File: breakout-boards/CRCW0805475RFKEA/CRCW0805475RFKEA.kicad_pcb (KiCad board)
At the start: 2 copper layers, 14 parts, among them J1 Conn_01x12, J2 Conn_01x12

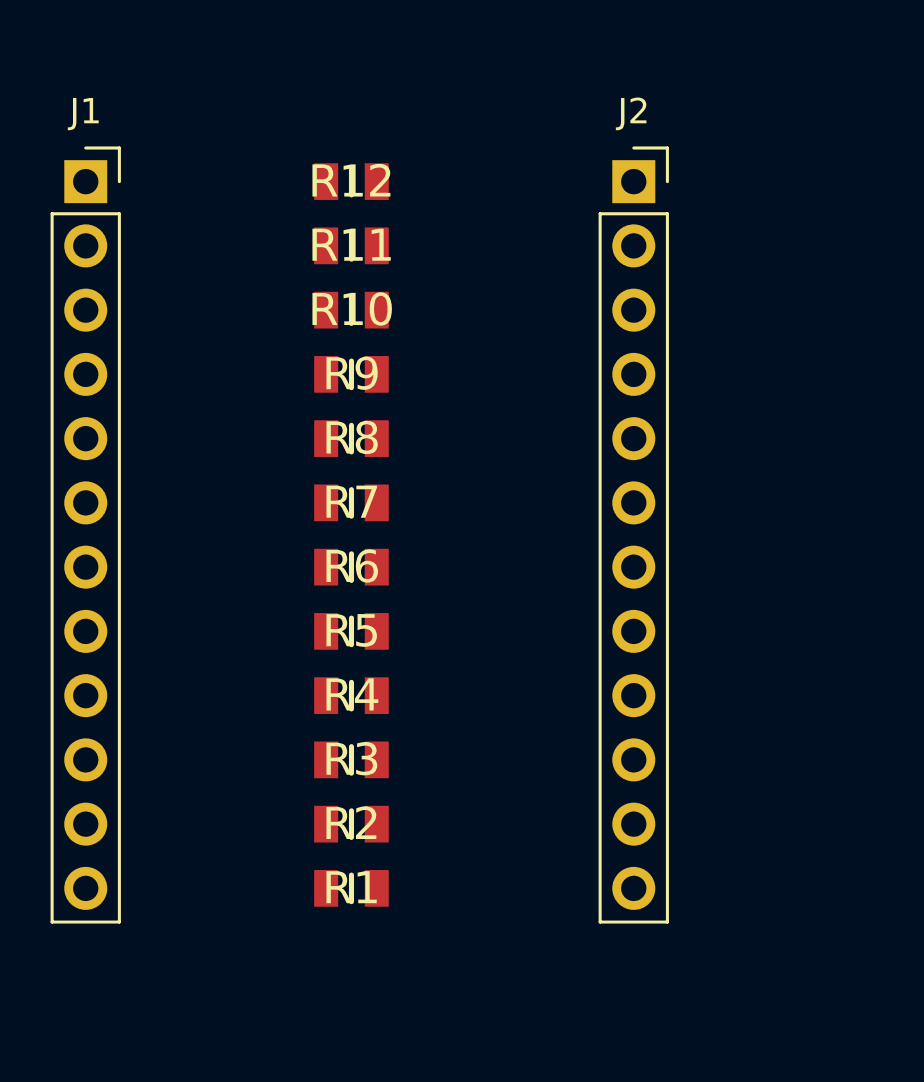
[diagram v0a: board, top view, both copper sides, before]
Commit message: feat: create footprints for resistor breakout boards
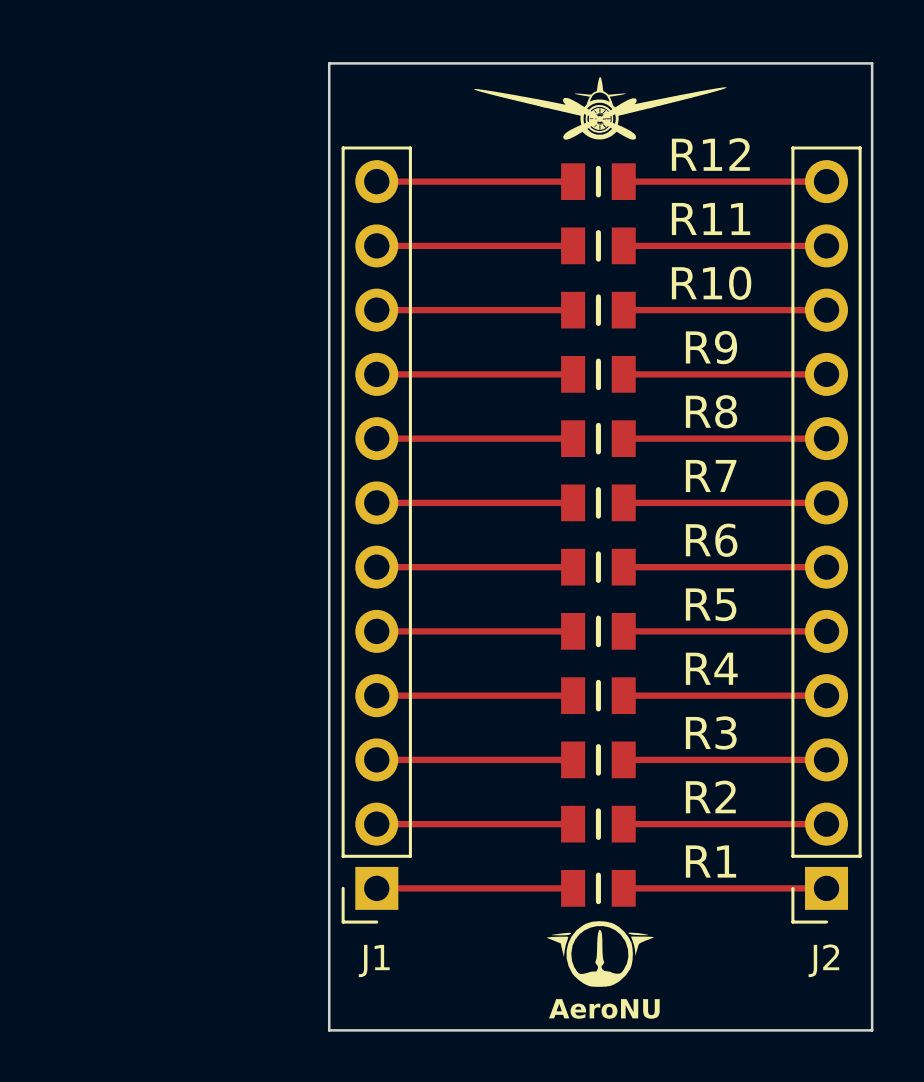
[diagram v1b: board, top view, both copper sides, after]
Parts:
- added AeroNU: LOGO, FixedWing:AeroNU - Logo (Smol), F.Cu at (161.4, 109.5)
- added FixedWing: LOGO, FixedWing:FixedWing - Logo (Smol), F.Cu at (161.3, 74.0)
- moved J1 30.2 mm to (152.4, 104.1), turned to 180 degrees
- moved J2 29.0 mm to (170.2, 104.1), turned to 180 degrees
- moved R1 9.76 mm to (161.2, 104.1)
- moved R10 9.76 mm to (161.2, 81.3)
- moved R11 9.76 mm to (161.2, 78.7)
- moved R12 9.76 mm to (161.2, 76.2)
- moved R2 9.76 mm to (161.2, 101.6)
- moved R3 9.76 mm to (161.2, 99.1)
- moved R4 9.76 mm to (161.2, 96.5)
- moved R5 9.76 mm to (161.2, 94.0)
- moved R6 9.76 mm to (161.2, 91.4)
- moved R7 9.76 mm to (161.2, 88.9)
- moved R8 9.76 mm to (161.2, 86.4)
- moved R9 9.76 mm to (161.2, 83.8)
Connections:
- R1 pad 1: Net-(J1-Pin_12) -> Net-(J1-Pin_1)
- R1 pad 2: Net-(J2-Pin_12) -> Net-(J2-Pin_1)
- R10 pad 1: Net-(J1-Pin_3) -> Net-(J1-Pin_10)
- R10 pad 2: Net-(J2-Pin_3) -> Net-(J2-Pin_10)
- R11 pad 1: Net-(J1-Pin_2) -> Net-(J1-Pin_11)
- R11 pad 2: Net-(J2-Pin_2) -> Net-(J2-Pin_11)
- R12 pad 1: Net-(J1-Pin_1) -> Net-(J1-Pin_12)
- R12 pad 2: Net-(J2-Pin_1) -> Net-(J2-Pin_12)
- R2 pad 1: Net-(J1-Pin_11) -> Net-(J1-Pin_2)
- R2 pad 2: Net-(J2-Pin_11) -> Net-(J2-Pin_2)
- R3 pad 1: Net-(J1-Pin_10) -> Net-(J1-Pin_3)
- R3 pad 2: Net-(J2-Pin_10) -> Net-(J2-Pin_3)
- R4 pad 1: Net-(J1-Pin_9) -> Net-(J1-Pin_4)
- R4 pad 2: Net-(J2-Pin_9) -> Net-(J2-Pin_4)
- R5 pad 1: Net-(J1-Pin_8) -> Net-(J1-Pin_5)
- R5 pad 2: Net-(J2-Pin_8) -> Net-(J2-Pin_5)
- R6 pad 1: Net-(J1-Pin_7) -> Net-(J1-Pin_6)
- R6 pad 2: Net-(J2-Pin_7) -> Net-(J2-Pin_6)
- R7 pad 1: Net-(J1-Pin_6) -> Net-(J1-Pin_7)
- R7 pad 2: Net-(J2-Pin_6) -> Net-(J2-Pin_7)
- R8 pad 1: Net-(J1-Pin_5) -> Net-(J1-Pin_8)
- R8 pad 2: Net-(J2-Pin_5) -> Net-(J2-Pin_8)
- R9 pad 1: Net-(J1-Pin_4) -> Net-(J1-Pin_9)
- R9 pad 2: Net-(J2-Pin_4) -> Net-(J2-Pin_9)
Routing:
- net Net-(J2-Pin_9): track 0.00 -> 8.02 mm
- net Net-(J2-Pin_8): track 0.00 -> 8.02 mm
- net Net-(J2-Pin_7): track 0.00 -> 8.02 mm
- net Net-(J2-Pin_6): track 0.00 -> 8.02 mm
- net Net-(J2-Pin_5): track 0.00 -> 8.02 mm
- net Net-(J2-Pin_4): track 0.00 -> 8.02 mm
- net Net-(J2-Pin_3): track 0.00 -> 8.02 mm
- net Net-(J2-Pin_2): track 0.00 -> 8.02 mm
- net Net-(J2-Pin_12): track 0.00 -> 8.02 mm
- net Net-(J2-Pin_11): track 0.00 -> 8.02 mm
- net Net-(J2-Pin_10): track 0.00 -> 8.02 mm
- net Net-(J2-Pin_1): track 0.00 -> 8.02 mm
- net Net-(J1-Pin_9): track 0.00 -> 7.76 mm
- net Net-(J1-Pin_8): track 0.00 -> 7.76 mm
- net Net-(J1-Pin_7): track 0.00 -> 7.76 mm
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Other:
- board outline added: 21.5 x 38.2 mm
- board text added: "AeroNU"
- board text added: "Designed By Ephram CJ and Matthew F"

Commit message: feat: finalize 470ohm board design
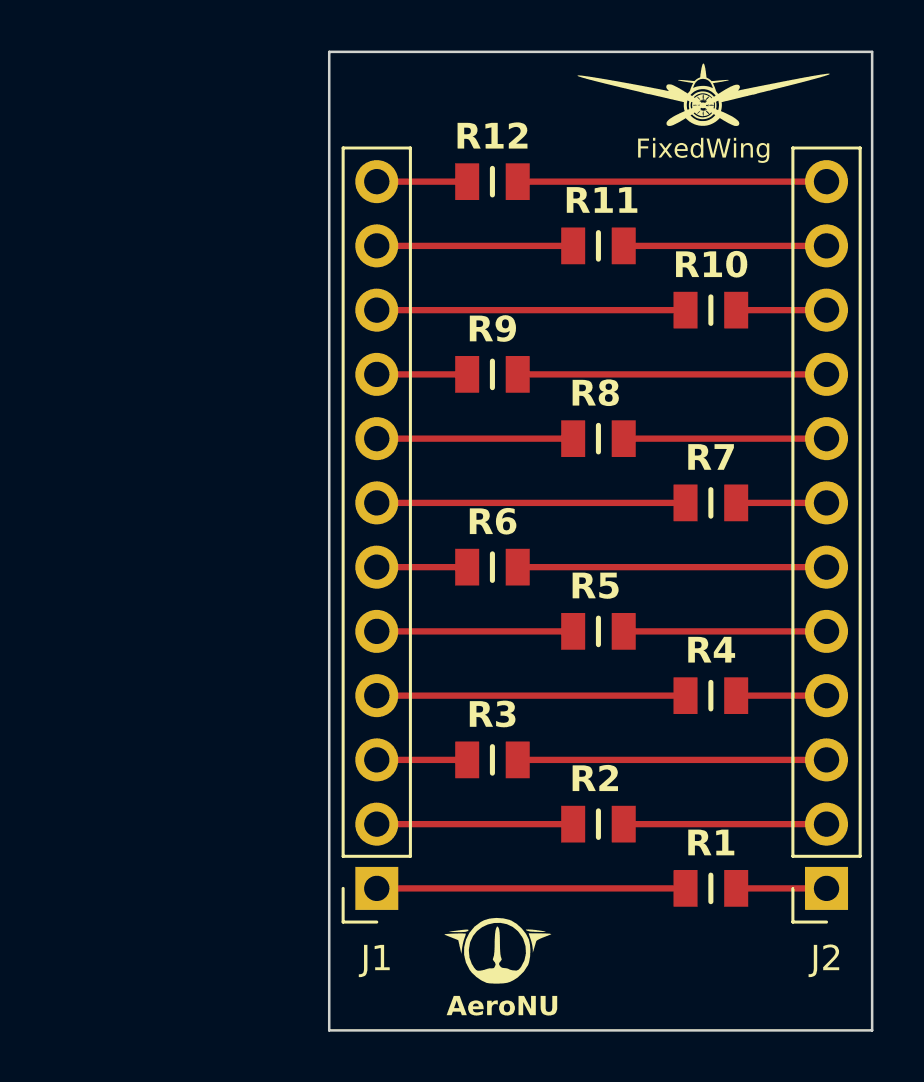
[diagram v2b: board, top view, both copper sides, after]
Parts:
- moved R1 4.44 mm to (165.6, 104.1)
- moved R10 4.44 mm to (165.6, 81.3)
- moved R4 4.44 mm to (165.6, 96.5)
- moved R7 4.44 mm to (165.6, 88.9)
- moved R12 4.19 mm to (157.0, 76.2)
- moved R3 4.19 mm to (157.0, 99.1)
- moved R6 4.19 mm to (157.0, 91.4)
- moved R9 4.19 mm to (157.0, 83.8)
- moved FixedWing 4.14 mm to (165.3, 73.2)
- moved AeroNU 4.05 mm to (157.3, 109.4)
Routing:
- net Net-(J2-Pin_7): track 8.02 -> 3.57 mm
- net Net-(J2-Pin_4): track 8.02 -> 3.57 mm
- net Net-(J2-Pin_10): track 8.02 -> 3.57 mm
- net Net-(J2-Pin_1): track 8.02 -> 3.57 mm
- net Net-(J1-Pin_7): track 7.76 -> 12.2 mm
- net Net-(J1-Pin_4): track 7.76 -> 12.2 mm
- net Net-(J1-Pin_10): track 7.76 -> 12.2 mm
- net Net-(J1-Pin_1): track 7.76 -> 12.2 mm
- net Net-(J2-Pin_9): track 8.02 -> 12.2 mm
- net Net-(J2-Pin_6): track 8.02 -> 12.2 mm
- net Net-(J2-Pin_3): track 8.02 -> 12.2 mm
- net Net-(J2-Pin_12): track 8.02 -> 12.2 mm
- net Net-(J1-Pin_9): track 7.76 -> 3.57 mm
- net Net-(J1-Pin_6): track 7.76 -> 3.57 mm
- net Net-(J1-Pin_3): track 7.76 -> 3.57 mm
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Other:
- board size 21.5 x 38.2 mm -> 21.5 x 38.7 mm
